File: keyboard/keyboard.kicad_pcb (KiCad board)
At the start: 2 copper layers, 127.1 x 77.5 mm, 22 parts

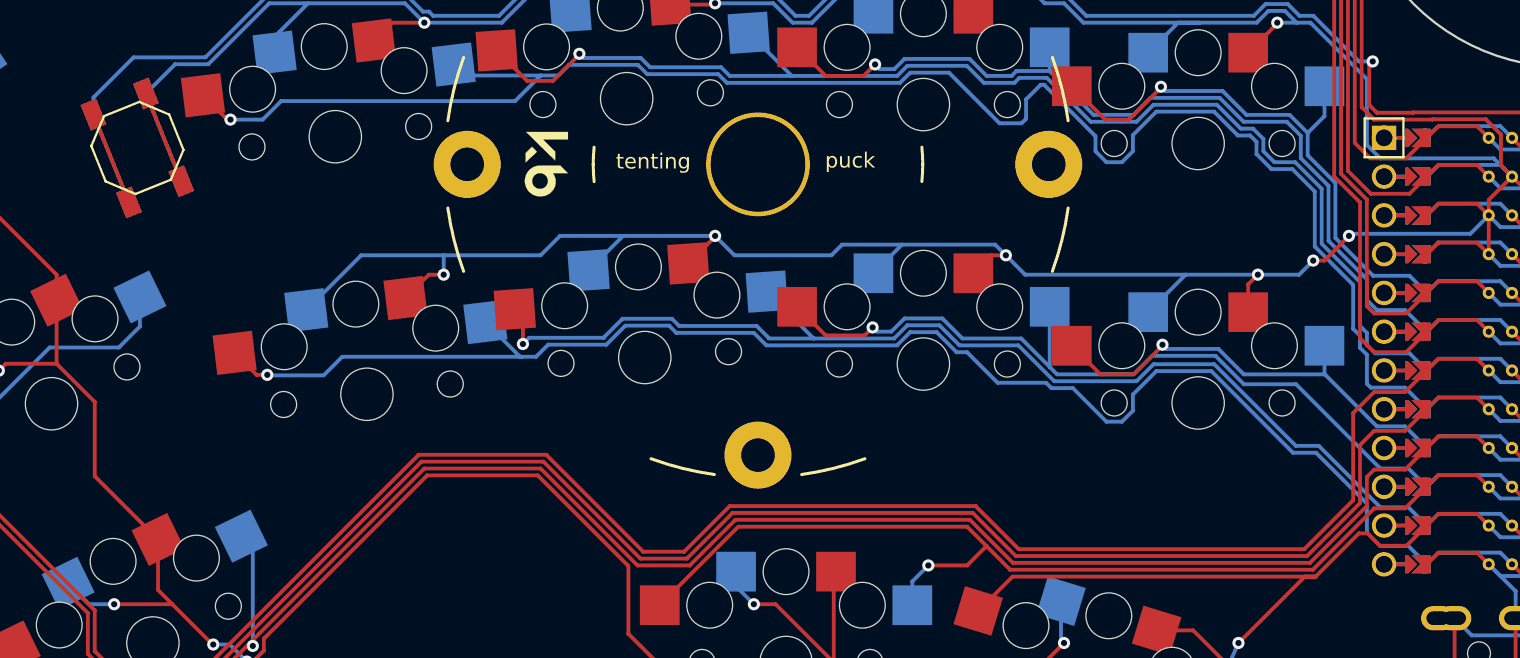
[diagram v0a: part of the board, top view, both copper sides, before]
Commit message: Fix a few issues
A clearance issue, and the reset pads on the opposite sides not
connected to each other.
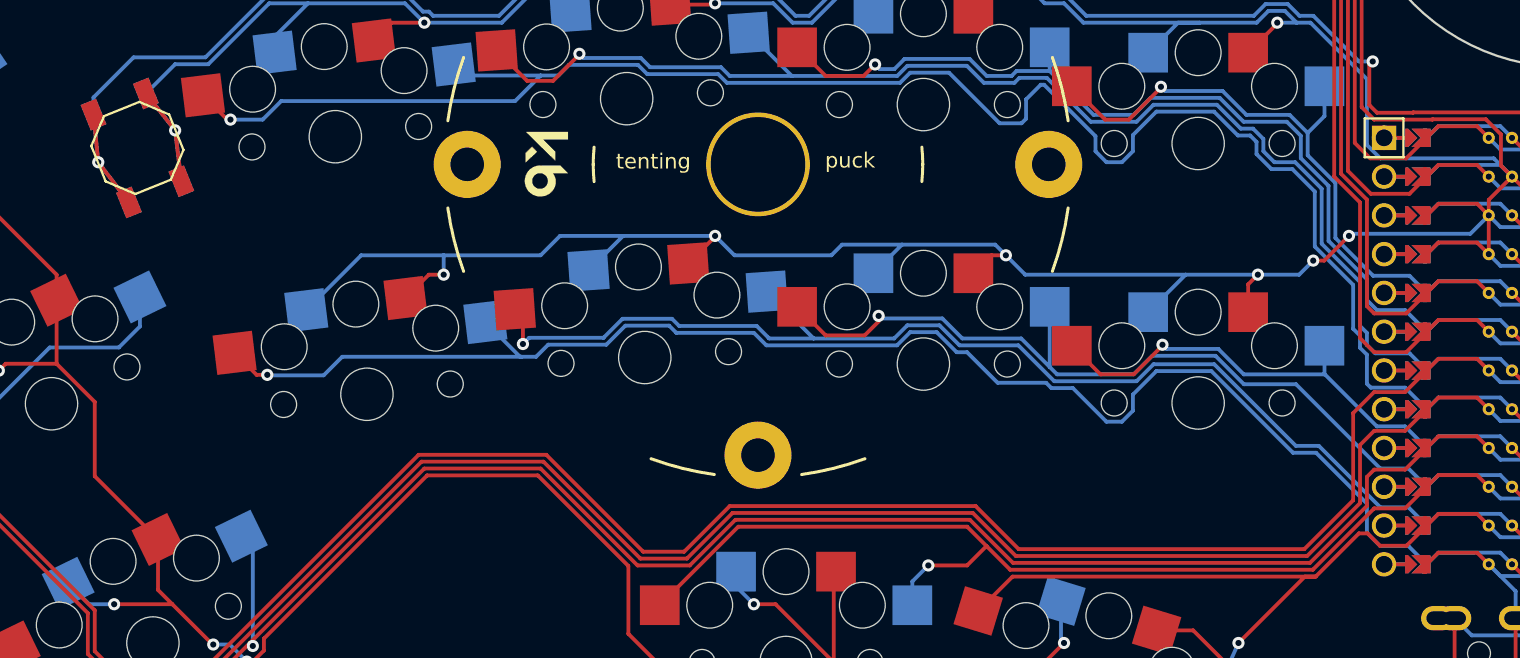
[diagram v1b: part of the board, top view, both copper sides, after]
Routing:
- net RST: track 136.9 -> 137.4 mm, vias 1 -> 2
- net GND: track 627.6 -> 628.1 mm, vias 21 -> 22

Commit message: Remake keyboard
It seems like there is some problem with the kicad project now
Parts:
- removed REF**: Tenting Puck, Library:TentingPuck
- added D1: , ComboDiode, F.Cu at (179.7, 140.4)
- added D10: , ComboDiode, F.Cu at (228.0, 122.6)
- added D11: , ComboDiode, F.Cu at (228.0, 105.6)
- added D12: , ComboDiode, F.Cu at (228.0, 88.6)
- added D13: , ComboDiode, F.Cu at (246.0, 125.2)
- added D14: , ComboDiode, F.Cu at (246.0, 108.2)
- added D15: , ComboDiode, F.Cu at (246.0, 91.2)
- added D16: , ComboDiode, F.Cu at (219.0, 142.2)
- added D17: , ComboDiode, F.Cu at (237.0, 144.6)
- added D18: , ComboDiode, F.Cu at (254.2, 152.1)
- added D2: , ComboDiode, F.Cu at (173.1, 124.7)
- added D3: , ComboDiode, F.Cu at (164.3, 109.5)
- added D4: , ComboDiode, F.Cu at (192.2, 124.6)
- added D5: , ComboDiode, F.Cu at (190.1, 107.7)
- added D6: , ComboDiode, F.Cu at (188.0, 90.8)
- added D7: , ComboDiode, F.Cu at (210.1, 122.2)
- added D8: , ComboDiode, F.Cu at (208.9, 105.2)
- added D9: , ComboDiode, F.Cu at (207.8, 88.3)
- added S18: , PG1350, F.Cu at (256.8, 147.9)
- moved S13 223.6 mm to (246.0, 120.2)
- moved S14 223.6 mm to (246.0, 103.2)
- moved S15 223.6 mm to (246.0, 86.2)
- moved TRRS1 223.6 mm to (273.0, 138.9)
- moved _1 223.6 mm to (265.8, 116.8)
- moved B1 223.6 mm to (176.5, 103.5)
- moved B2 223.6 mm to (176.5, 103.5)
- moved S3 223.6 mm to (161.5, 105.4)
- moved S2 223.6 mm to (170.9, 120.2)
- moved S9 223.6 mm to (207.4, 83.3)
- moved S8 223.6 mm to (208.6, 100.3)
- moved S7 223.6 mm to (209.8, 117.2)
- moved S1 223.6 mm to (177.6, 135.9)
- moved S17 223.6 mm to (238.4, 139.8)
- moved S5 223.6 mm to (189.5, 102.8)
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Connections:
- B1 pad 1: RST -> GND
- B1 pad 2: GND -> RST
- S1 pad 1: GND -> B1
- S1 pad 2: main_pinkie_bottom -> pinkie_bottom
- S10 pad 1: GND -> F5
- S10 pad 2: main_index_bottom -> index_bottom
- S11 pad 1: GND -> F5
- S11 pad 2: main_index_home -> index_home
- S12 pad 1: GND -> F5
- S12 pad 2: main_index_top -> index_top
- S13 pad 1: GND -> F4
- S13 pad 2: main_far_bottom -> far_bottom
- S14 pad 1: GND -> F4
- S14 pad 2: main_far_home -> far_home
- S15 pad 1: GND -> F4
- S15 pad 2: main_far_top -> far_top
- S16 pad 1: GND -> F6
- S16 pad 2: thumb_tucky -> tucky_thumb
- S17 pad 1: GND -> F5
- S17 pad 2: thumb_resty -> resty_thumb
- S2 pad 1: GND -> B1
- S2 pad 2: main_pinkie_home -> pinkie_home
- S3 pad 1: GND -> B1
- S3 pad 2: main_pinkie_top -> pinkie_top
- S4 pad 1: GND -> F7
- S4 pad 2: main_ring_bottom -> ring_bottom
- S5 pad 1: GND -> F7
- S5 pad 2: main_ring_home -> ring_home
- S6 pad 1: GND -> F7
- S6 pad 2: main_ring_top -> ring_top
- S7 pad 1: GND -> F6
- S7 pad 2: main_middle_bottom -> middle_bottom
- S8 pad 1: GND -> F6
- S8 pad 2: main_middle_home -> middle_home
- S9 pad 1: GND -> F6
- S9 pad 2: main_middle_top -> middle_top
- TRRS1 pad 3: P9 -> VCC
- TRRS1 pad 4: VCC -> D2
- _1 pad 10: main_index_bottom -> B3
- _1 pad 11: main_middle_bottom -> B2
- _1 pad 12: main_ring_bottom -> B6
- _1 pad 13: P9 -> B5
- _1 pad 14: thumb_resty -> B5
- _1 pad 15: thumb_tucky -> E6
- _1 pad 16: main_pinkie_bottom -> D7
- _1 pad 17: main_pinkie_home -> C6
- _1 pad 18: main_pinkie_top -> D4
- _1 pad 19: main_ring_top -> D0
- _1 pad 20: main_middle_top -> D1
- _1 pad 23: main_index_top -> D2
- _1 pad 24: main_far_top -> D3
- _1 pad 5: main_far_home -> F4
- _1 pad 6: main_index_home -> F5
- _1 pad 7: main_middle_home -> F6
- _1 pad 8: main_ring_home -> F7
- _1 pad 9: main_far_bottom -> B1
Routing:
- net GND: track 628.1 -> 0.00 mm, vias 22 -> 0
- net main_pinkie_top: track 167.9 -> 0.00 mm, vias 1 -> 0
- net main_pinkie_home: track 144.9 -> 0.00 mm, vias 1 -> 0
- net RST: track 137.4 -> 0.00 mm, vias 2 -> 0
- net main_ring_top: track 123.1 -> 0.00 mm, vias 1 -> 0
- net main_pinkie_bottom: track 115.9 -> 0.00 mm, vias 1 -> 0
- net main_ring_home: track 109.8 -> 0.00 mm, vias 1 -> 0
- net main_middle_top: track 100.4 -> 0.00 mm, vias 1 -> 0
- net main_ring_bottom: track 95.0 -> 0.00 mm, vias 1 -> 0
- net main_middle_home: track 81.6 -> 0.00 mm, vias 1 -> 0
- net main_middle_bottom: track 73.2 -> 0.00 mm, vias 1 -> 0
- net main_index_top: track 69.4 -> 0.00 mm, vias 1 -> 0
- net thumb_tucky: track 63.2 -> 0.00 mm, vias 1 -> 0
- net main_index_home: track 56.7 -> 0.00 mm, vias 1 -> 0
- net main_index_bottom: track 52.4 -> 0.00 mm, vias 1 -> 0
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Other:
- board size 127.1 x 77.5 mm -> 134.3 x 93.3 mm
- net class Default added: clearance 0.2, trace_width 0.25, via_dia 0.8, via_drill 0.4

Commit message: Fix reset button orientation
For easier and prettier routing
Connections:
- B2 pad 1: RST -> GND
- B2 pad 2: GND -> RST
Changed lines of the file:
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@@
         (fp_line (start -2.75 -1.25) (end -1.25 -2.75) (layer B.SilkS) (width 0.15))
         (fp_line (start -2.75 -1.25) (end -2.75 1.25) (layer B.SilkS) (width 0.15))
-        (pad 1 smd rect (at -3.1 -1.85 112) (size 1.8 1.1) (layers B.Cu B.Paste B.Mask) (net 30 "RST"))
-        (pad 1 smd rect (at 3.1 -1.85 112) (size 1.8 1.1) (layers B.Cu B.Paste B.Mask) (net 30 "RST"))
-        (pad 2 smd rect (at -3.1 1.85 112) (size 1.8 1.1) (layers B.Cu B.Paste B.Mask) (net 29 "GND"))
-        (pad 2 smd rect (at 3.1 1.85 112) (size 1.8 1.1) (layers B.Cu B.Paste B.Mask) (net 29 "GND"))
+        (pad 1 smd rect (at -3.1 -1.85 112) (size 1.8 1.1) (layers B.Cu B.Paste B.Mask) (net 29 "GND"))
+        (pad 1 smd rect (at 3.1 -1.85 112) (size 1.8 1.1) (layers B.Cu B.Paste B.Mask) (net 29 "GND"))
+        (pad 2 smd rect (at -3.1 1.85 112) (size 1.8 1.1) (layers B.Cu B.Paste B.Mask) (net 30 "RST"))
+        (pad 2 smd rect (at 3.1 1.85 112) (size 1.8 1.1) (layers B.Cu B.Paste B.Mask) (net 30 "RST"))
     )
   (gr_line (start 175.8438196 150.6631511) (end 188.12959262977836 144.67097925895655) (angle 90) (layer Edge.Cuts) (width 0.15))

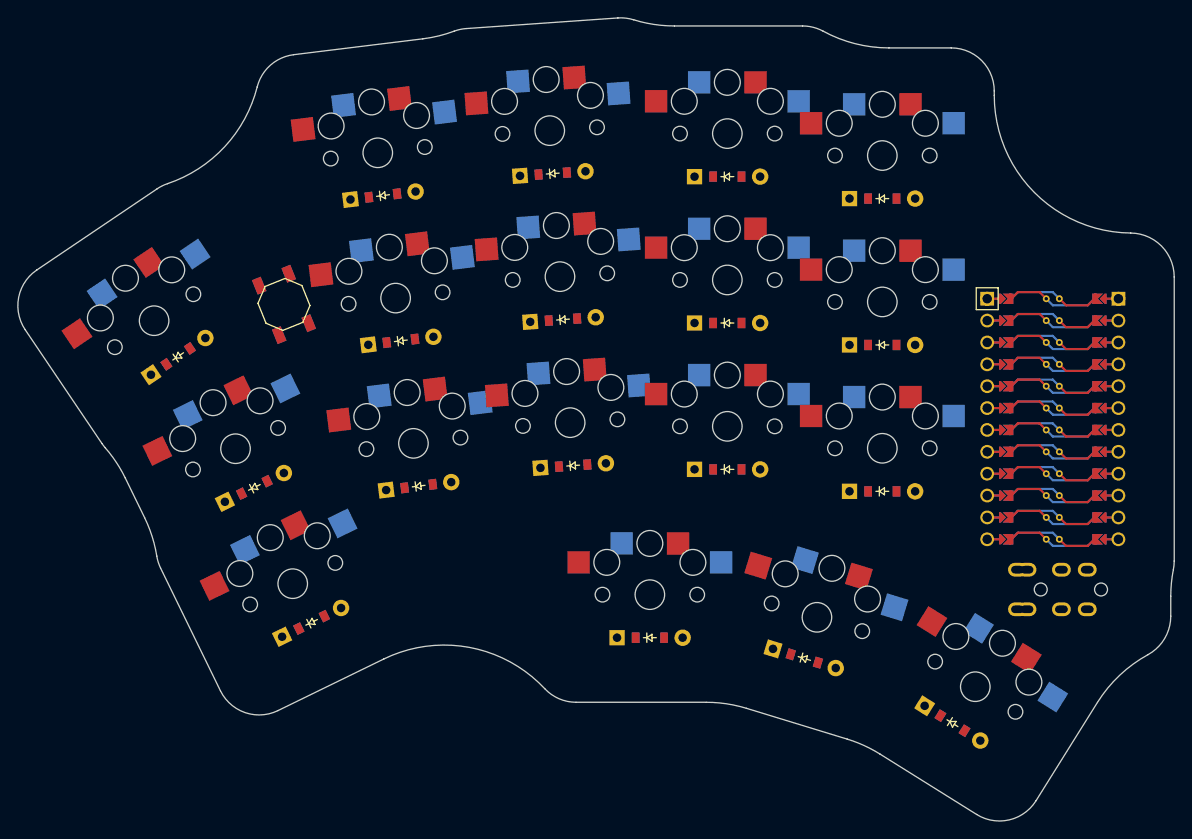
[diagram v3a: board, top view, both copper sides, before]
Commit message: Add connections on PCB
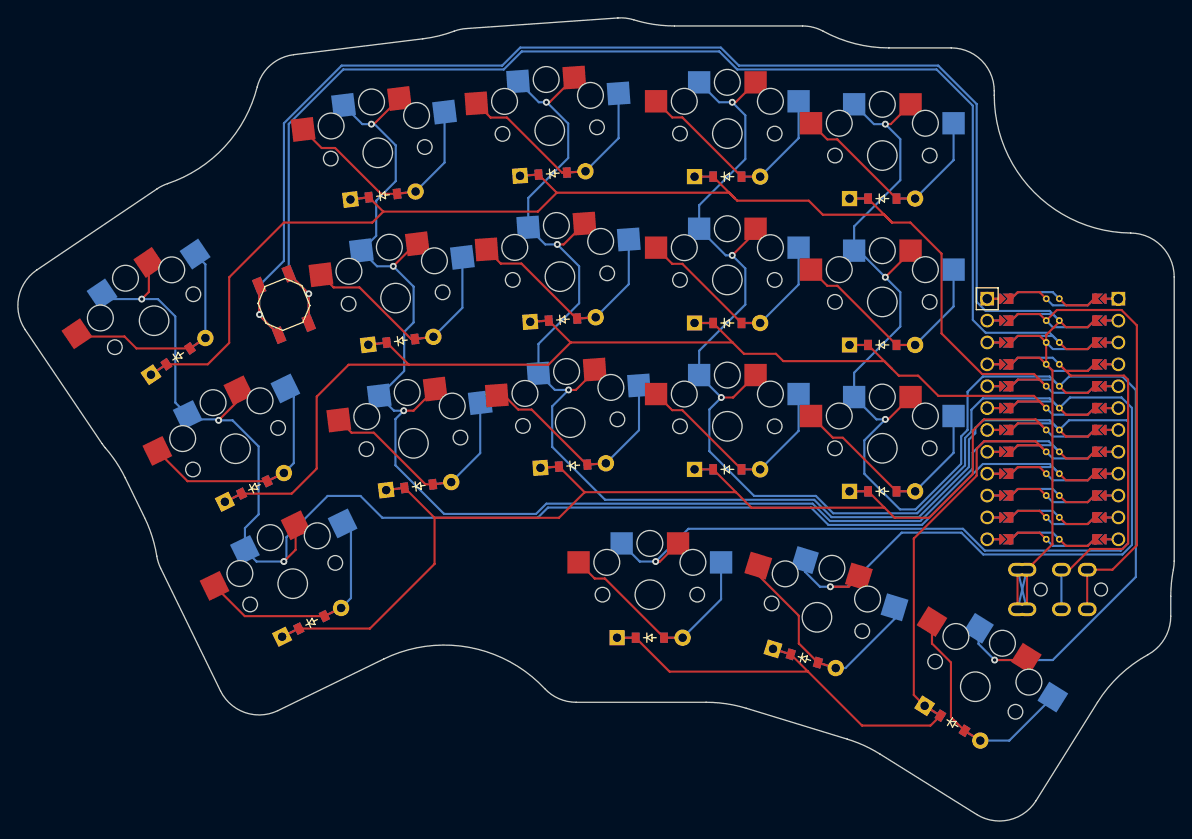
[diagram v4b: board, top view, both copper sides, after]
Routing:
- net F6: track 0.00 -> 226.7 mm, vias 0 -> 4
- net GND: track 0.00 -> 203.4 mm, vias 0 -> 1
- net F5: track 0.00 -> 193.5 mm, vias 0 -> 4
- net D1: track 0.00 -> 164.1 mm
- net F4: track 0.00 -> 163.2 mm, vias 0 -> 4
- net B1: track 0.00 -> 160.7 mm, vias 0 -> 3
- net F7: track 0.00 -> 153.4 mm, vias 0 -> 3
- net RST: track 0.00 -> 152.4 mm, vias 0 -> 1
- net D0: track 0.00 -> 144.7 mm
- net D4: track 0.00 -> 143.1 mm
- net C6: track 0.00 -> 98.3 mm
- net D2: track 0.00 -> 48.8 mm
- net VCC: track 0.00 -> 40.4 mm
- net pinkie_home: track 0.00 -> 29.2 mm
- net pinkie_bottom: track 0.00 -> 29.2 mm
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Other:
- net class Default removed

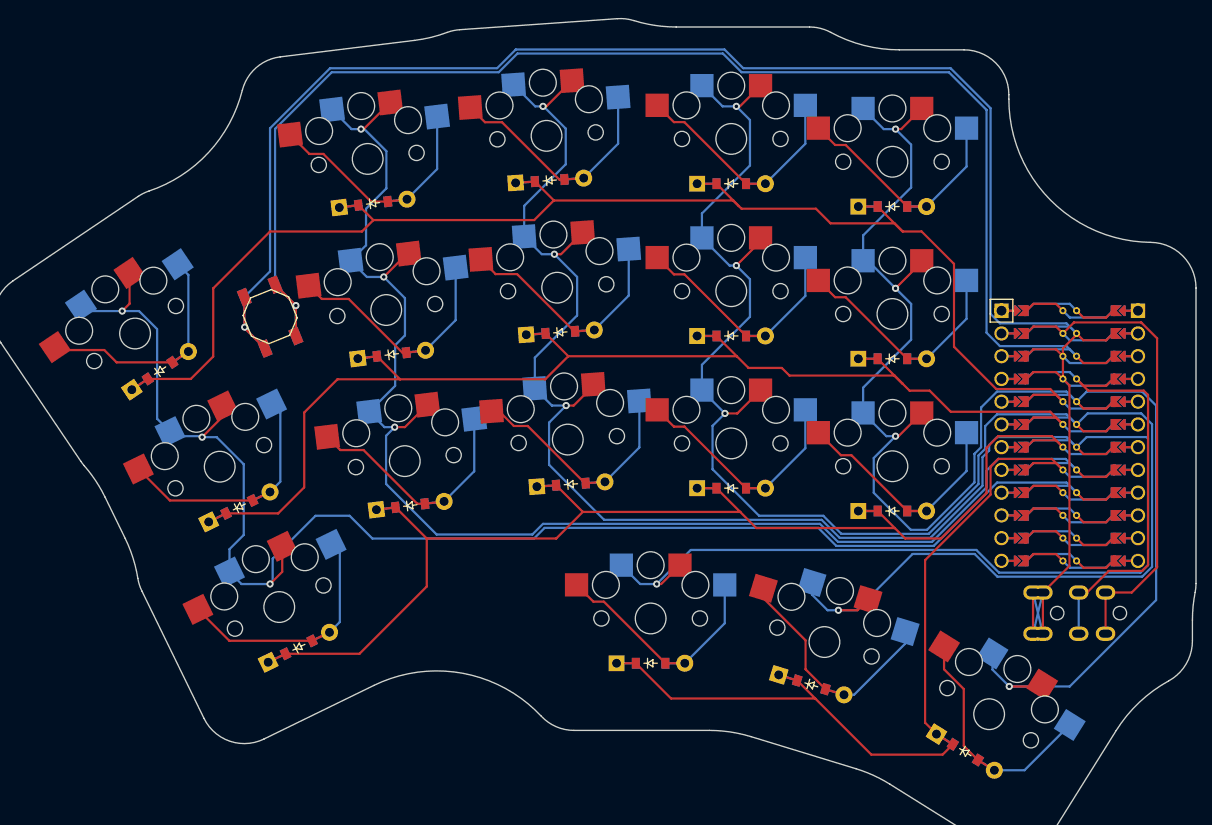
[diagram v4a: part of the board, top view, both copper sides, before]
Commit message: Fix a wrong connection on MCU, rewire PCB
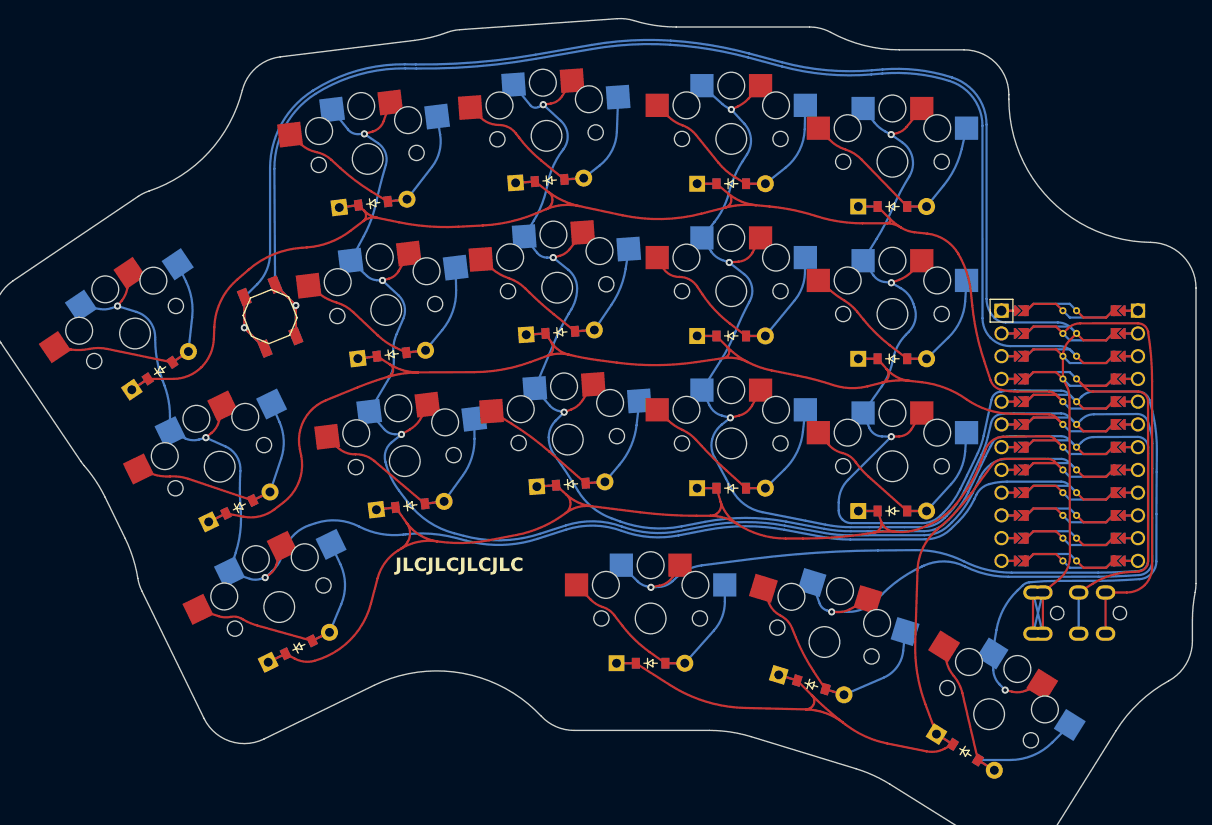
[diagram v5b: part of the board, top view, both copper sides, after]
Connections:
- _1 pad 14: B5 -> B4
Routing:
- net D4: track 143.1 -> 150.5 mm
- net D0: track 144.7 -> 150.8 mm
- net D1: track 164.1 -> 169.6 mm
- net F6: track 226.7 -> 221.3 mm
- net F5: track 193.5 -> 188.6 mm
- net B1: track 160.7 -> 156.4 mm
- net GND: track 203.4 -> 199.3 mm
- net F4: track 163.2 -> 167.1 mm
- net RST: track 152.4 -> 148.8 mm
- net C6: track 98.3 -> 101.6 mm
- net F7: track 153.4 -> 150.2 mm
- net pinkie_home: track 29.2 -> 26.3 mm
- net ring_home: track 29.0 -> 26.4 mm
- net middle_home: track 28.5 -> 26.0 mm
- net index_home: track 28.5 -> 26.9 mm
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- added copper zone on F.Cu, net C6
- added copper zone on F.Cu, net D0
- added copper zone on F.Cu, net D1
- added copper zone on F.Cu, net D4
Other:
- board text added: "JLCJLCJLCJLC"
